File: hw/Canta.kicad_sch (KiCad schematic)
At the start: 50 parts, among them J1 USB_C_Receptacle_PowerOnly_6P, J101 Conn_01x01, J102 Conn_01x01, J103 Conn_01x01, J104 Conn_01x01, J105 Conn_01x01, J106 Conn_01x01, J107 Conn_01x01, J108 Conn_01x01, J109 Conn_01x01, J110 Conn_01x01, J111 Conn_01x01, J112 Conn_01x01, J2 Conn_01x04, U1 SPX3819M5-L-3-3, U2 PY32F003F18U6, U3 TM8211, U4 FM8002A, Y1 32MHz 12pF

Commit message: Fix thermal pad connection in PY32 symbol
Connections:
- net GND: now also U2.21 (PAD)
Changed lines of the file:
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@@
     (pin "8")
     (pin "9")
+    (pin "21")
     (instances
       (project "Canta"

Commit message: Layout, I think
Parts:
- removed J2: Conn_01x04, Canta_footprints:TestPoints_1x04_P2.0, symbol Connector_Generic:Conn_01x04
- added D1: Pink, LED_SMD:LED_0603_1608Metric, symbol Device:LED
- added J2: Conn_01x03, Canta_footprints:TestPoints_1x03_P2.0, symbol Connector_Generic:Conn_01x03
- added R3: 7.5k, Resistor_SMD:R_0402_1005Metric, symbol Device:R
- J101, J102, J103, J104, J105, J106, J107, J108, J109, J110: footprint TestPoint:TestPoint_Pad_4.0x4.0mm -> Canta_footprints:TouchPad_Keyboard
- J111, J112: footprint TestPoint:TestPoint_Pad_4.0x4.0mm -> Canta_footprints:TouchPad_Transpose
- JP1, JP2: footprint Jumper:SolderJumper-2_P1.3mm_Open_RoundedPad1.0x1.5mm -> Canta_footprints:SolderJumper-2_Open
- LS1: footprint Connector_PinHeader_2.00mm:PinHeader_1x02_P2.00mm_Vertical_SMD_Pin1Left -> Canta_footprints:Speaker_1x02_P2
- R6: renamed from R5; footprint Resistor_SMD:R_0402_1005Metric -> Potentiometer_SMD:Potentiometer_Bourns_TC33X_Vertical
- renumbered C5 to C4, C4 to C5, R3 to R4, R4 to R5
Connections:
- net +3.3V: now also D1.2 (A)
- net GND: now also J2.1 (Pin_1), R3.2
- net SWCLK: now also J2.2 (Pin_2)
- net SWDIO: now also J2.3 (Pin_3)
- new net: D1.1 (K), R3.1
- no-connect marks 3 -> 4

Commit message: Routing, I think
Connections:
- net BTN_01: now also U2.15 (PF2); no longer U2.16 (PA0)
- net BTN_02: now also U2.16 (PA0); no longer U2.18 (PA2)
- net BTN_03: now also U2.18 (PA2); no longer U2.19 (PA3)
- net BTN_04: now also U2.19 (PA3); no longer U2.20 (PA4)
- net BTN_05: now also U2.20 (PA4); no longer U2.1 (PA5)
- net BTN_06: now also U2.1 (PA5); no longer U2.2 (PA6)
- net BTN_07: now also U2.2 (PA6); no longer U2.3 (PA7)
- net BTN_08: now also U2.3 (PA7); no longer U2.5 (PA12)
- net BTN_09: now also U2.5 (PA12); no longer JP1.2 (B), U2.7 (PA13)
- net BTN_10: now also JP1.2 (B), U2.7 (PA13); no longer JP2.2 (B), U2.8 (PA14)
- net BTN_12: now also JP2.2 (B), U2.8 (PA14); no longer U2.15 (PF2)
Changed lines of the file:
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@@
     )
   )
-  (global_label "BTN_09" (shape bidirectional) (at 159.385 57.15 270) (fields_autoplaced)
+  (global_label "BTN_10" (shape bidirectional) (at 159.385 57.15 270) (fields_autoplaced)
     (effects (font (size 1.27 1.27)) (justify right))
     (property "Intersheetrefs" "${INTERSHEET_REFS}" (at 159.385 68.2012 90)
@@
     )
   )
-  (global_label "BTN_07" (shape bidirectional) (at 148.59 44.45 180) (fields_autoplaced)
+  (global_label "BTN_08" (shape bidirectional) (at 148.59 44.45 180) (fields_autoplaced)
     (effects (font (size 1.27 1.27)) (justify right))
     (property "Intersheetrefs" "${INTERSHEET_REFS}" (at 137.5388 44.45 0)
@@
     )
   )
-  (global_label "BTN_01" (shape bidirectional) (at 167.005 31.115 90) (fields_autoplaced)
+  (global_label "BTN_02" (shape bidirectional) (at 167.005 31.115 90) (fields_autoplaced)
     (effects (font (size 1.27 1.27)) (justify left))
     (property "Intersheetrefs" "${INTERSHEET_REFS}" (at 167.005 20.0638 90)
@@
     )
   )
-  (global_label "BTN_08" (shape bidirectional) (at 148.59 49.53 180) (fields_autoplaced)
+  (global_label "BTN_09" (shape bidirectional) (at 148.59 49.53 180) (fields_autoplaced)
     (effects (font (size 1.27 1.27)) (justify right))
     (property "Intersheetrefs" "${INTERSHEET_REFS}" (at 137.5388 49.53 0)
@@
     )
   )
-  (global_label "BTN_04" (shape bidirectional) (at 156.845 31.115 90) (fields_autoplaced)
+  (global_label "BTN_05" (shape bidirectional) (at 156.845 31.115 90) (fields_autoplaced)
     (effects (font (size 1.27 1.27)) (justify left))
     (property "Intersheetrefs" "${INTERSHEET_REFS}" (at 156.845 20.0638 90)
@@
     )
   )
-  (global_label "BTN_05" (shape bidirectional) (at 148.59 39.37 180) (fields_autoplaced)
+  (global_label "BTN_06" (shape bidirectional) (at 148.59 39.37 180) (fields_autoplaced)
     (effects (font (size 1.27 1.27)) (justify right))
     (property "Intersheetrefs" "${INTERSHEET_REFS}" (at 137.5388 39.37 0)
@@
     )
   )
-  (global_label "BTN_06" (shape bidirectional) (at 148.59 41.91 180) (fields_autoplaced)
+  (global_label "BTN_07" (shape bidirectional) (at 148.59 41.91 180) (fields_autoplaced)
     (effects (font (size 1.27 1.27)) (justify right))
     (property "Intersheetrefs" "${INTERSHEET_REFS}" (at 137.5388 41.91 0)
@@
     )
   )
-  (global_label "BTN_10" (shape bidirectional) (at 161.925 57.15 270) (fields_autoplaced)
+  (global_label "BTN_12" (shape bidirectional) (at 161.925 57.15 270) (fields_autoplaced)
     (effects (font (size 1.27 1.27)) (justify right))
     (property "Intersheetrefs" "${INTERSHEET_REFS}" (at 161.925 68.2012 90)
@@
     )
   )
-  (global_label "BTN_02" (shape bidirectional) (at 161.925 31.115 90) (fields_autoplaced)
+  (global_label "BTN_03" (shape bidirectional) (at 161.925 31.115 90) (fields_autoplaced)
     (effects (font (size 1.27 1.27)) (justify left))
     (property "Intersheetrefs" "${INTERSHEET_REFS}" (at 161.925 20.0638 90)
@@
     )
   )
-  (global_label "BTN_03" (shape bidirectional) (at 159.385 31.115 90) (fields_autoplaced)
+  (global_label "BTN_04" (shape bidirectional) (at 159.385 31.115 90) (fields_autoplaced)
     (effects (font (size 1.27 1.27)) (justify left))
     (property "Intersheetrefs" "${INTERSHEET_REFS}" (at 159.385 20.0638 90)
@@
     )
   )
-  (global_label "BTN_12" (shape bidirectional) (at 174.625 39.37 0) (fields_autoplaced)
+  (global_label "BTN_01" (shape bidirectional) (at 174.625 39.37 0) (fields_autoplaced)
     (effects (font (size 1.27 1.27)) (justify left))
     (property "Intersheetrefs" "${INTERSHEET_REFS}" (at 185.6762 39.37 0)

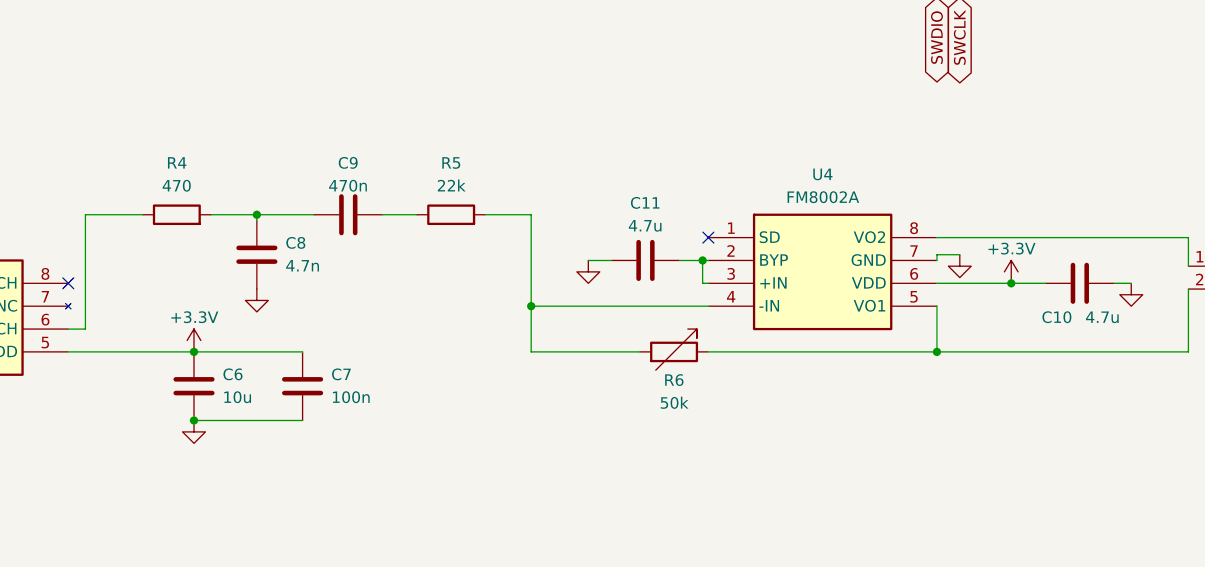
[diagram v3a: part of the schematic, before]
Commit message: Switch supplies of audio ICs to 5 V
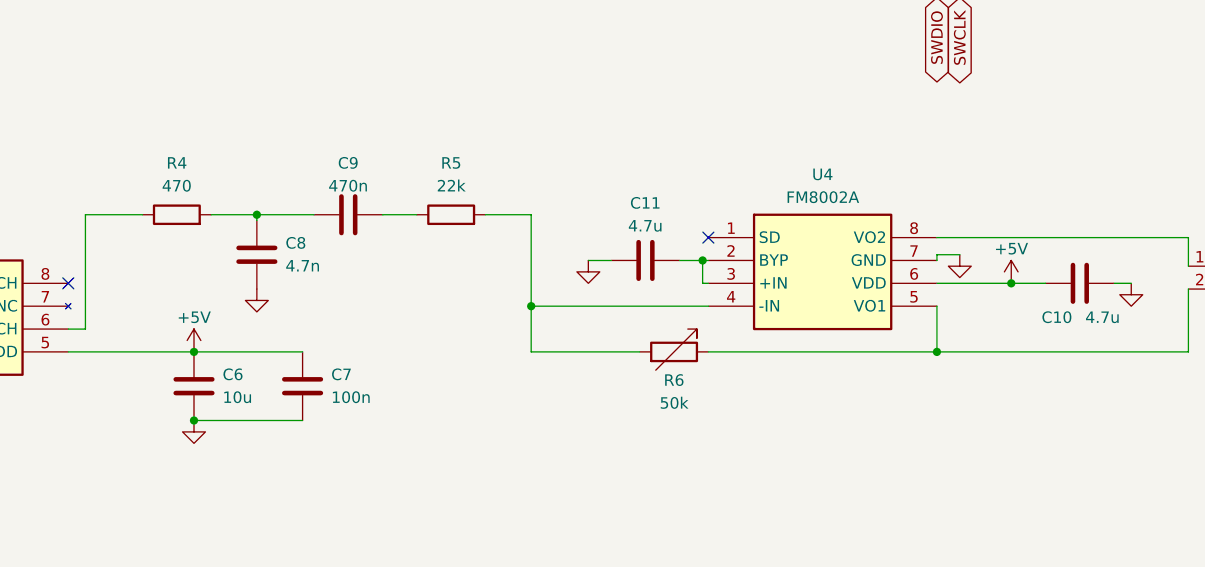
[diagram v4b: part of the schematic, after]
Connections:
- net +3.3V: no longer C10.1, C6.1, C7.1, U3.5 (VDD), U4.6 (VDD)
- net +5V: now also C10.1, C6.1, C7.1, U3.5 (VDD), U4.6 (VDD)

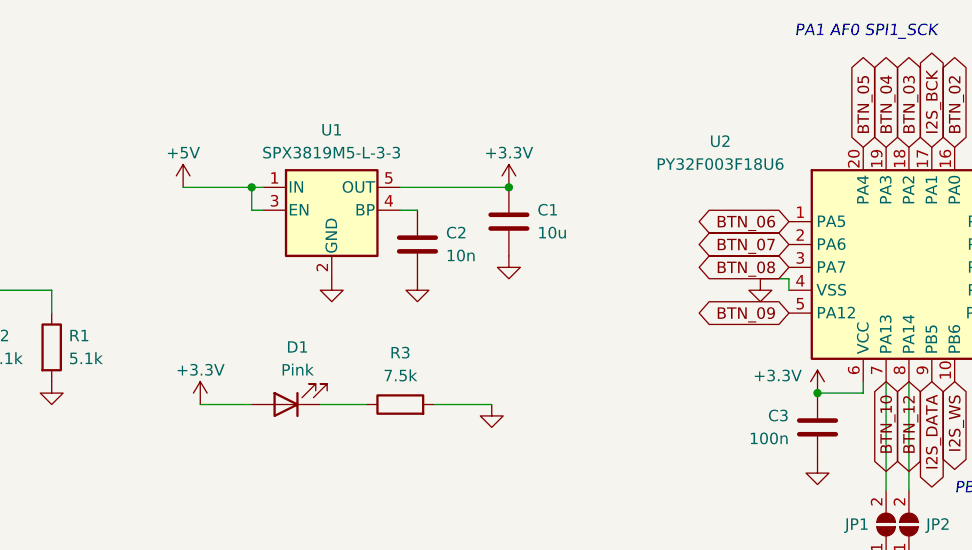
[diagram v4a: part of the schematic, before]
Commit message: Modify entire circuit to run on 5 V
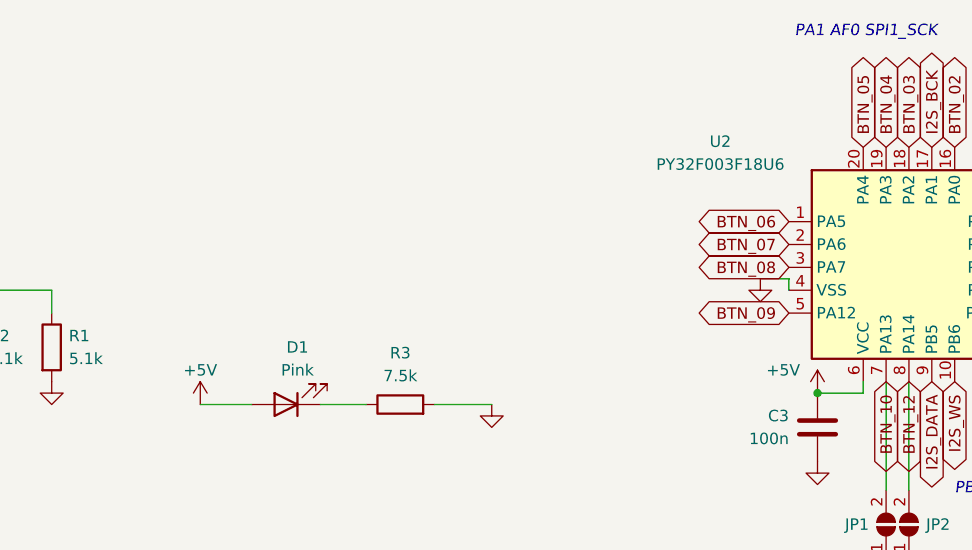
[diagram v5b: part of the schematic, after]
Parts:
- removed C1: 10u, Capacitor_SMD:C_0603_1608Metric, symbol Device:C
- removed C2: 10n, Capacitor_SMD:C_0402_1005Metric, symbol Device:C
- removed U1: SPX3819M5-L-3-3, Package_TO_SOT_SMD:SOT-23-5, symbol Regulator_Linear:SPX3819M5-L-3-3
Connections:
- net +3.3V: no longer C3.1, D1.2 (A), U2.6 (VCC)
- net +5V: now also C3.1, D1.2 (A), U2.6 (VCC)

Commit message: Update silkscreen
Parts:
- R3: value 7.5k -> 10k
- renumbered C3 to C1, C4 to C2, C5 to C3, C6 to C4, C7 to C5, C8 to C6, C9 to C7, C10 to C8, C11 to C9, U2 to U1, U3 to U2, U4 to U3
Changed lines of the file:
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@@
       (effects (font (size 1.27 1.27)))
     )
-    (property "Value" "7.5k" (at 105.41 56.515 90)
+    (property "Value" "10k" (at 105.41 56.515 90)
       (effects (font (size 1.27 1.27)))
     )
@@
   (symbol (lib_id "Device:C") (at 88.9 120.015 0) (unit 1)
     (in_bom yes) (on_board yes) (dnp no)
-    (property "Reference" "C7" (at 92.075 118.745 0)
+    (property "Reference" "C5" (at 92.075 118.745 0)
       (effects (font (size 1.27 1.27)) (justify left))
     )
@@
       (project "Canta"
         (path "/0da9ae68-938f-47fa-aa31-df1300665123"
-          (reference "C7") (unit 1)
+          (reference "C5") (unit 1)
         )
       )
@@
   (symbol (lib_id "Device:C") (at 76.835 120.015 0) (unit 1)
     (in_bom yes) (on_board yes) (dnp no)
-    (property "Reference" "C6" (at 80.01 118.745 0)
+    (property "Reference" "C4" (at 80.01 118.745 0)
       (effects (font (size 1.27 1.27)) (justify left))
     )
@@
       (project "Canta"
         (path "/0da9ae68-938f-47fa-aa31-df1300665123"
-          (reference "C6") (unit 1)
+          (reference "C4") (unit 1)
         )
       )
@@
   (symbol (lib_id "Device:C") (at 175.26 108.585 90) (unit 1)
     (in_bom yes) (on_board yes) (dnp no)
-    (property "Reference" "C10" (at 172.72 112.395 90)
+    (property "Reference" "C8" (at 172.72 112.395 90)
       (effects (font (size 1.27 1.27)))
     )
@@
       (project "Canta"
         (path "/0da9ae68-938f-47fa-aa31-df1300665123"
-          (reference "C10") (unit 1)
+          (reference "C8") (unit 1)
         )
       )
@@
   (symbol (lib_id "Canta_symbols:PY32F003F18U6TR") (at 161.925 44.45 0) (unit 1)
     (in_bom yes) (on_board yes) (dnp no)
-    (property "Reference" "U2" (at 140.97 30.48 0)
+    (property "Reference" "U1" (at 140.97 30.48 0)
       (effects (font (size 1.27 1.27)))
     )
@@
       (project "Canta"
         (path "/0da9ae68-938f-47fa-aa31-df1300665123"
-          (reference "U2") (unit 1)
+          (reference "U1") (unit 1)
         )
       )
@@
   (symbol (lib_id "Device:C") (at 151.765 62.23 0) (mirror y) (unit 1)
     (in_bom yes) (on_board yes) (dnp no)
-    (property "Reference" "C3" (at 148.59 60.96 0)
+    (property "Reference" "C1" (at 148.59 60.96 0)
       (effects (font (size 1.27 1.27)) (justify left))
     )
@@
       (project "Canta"
         (path "/0da9ae68-938f-47fa-aa31-df1300665123"
-          (reference "C3") (unit 1)
+          (reference "C1") (unit 1)
         )
       )
@@
   (symbol (lib_id "Device:C") (at 127 106.045 90) (unit 1)
     (in_bom yes) (on_board yes) (dnp no)
-    (property "Reference" "C11" (at 127 99.695 90)
+    (property "Reference" "C9" (at 127 99.695 90)
       (effects (font (size 1.27 1.27)))
     )
@@
       (project "Canta"
         (path "/0da9ae68-938f-47fa-aa31-df1300665123"
-          (reference "C11") (unit 1)
+          (reference "C9") (unit 1)
         )
       )
@@
   (symbol (lib_id "Device:C") (at 83.82 105.41 0) (unit 1)
     (in_bom yes) (on_board yes) (dnp no)
-    (property "Reference" "C8" (at 86.995 104.14 0)
+    (property "Reference" "C6" (at 86.995 104.14 0)
       (effects (font (size 1.27 1.27)) (justify left))
     )
@@
       (project "Canta"
         (path "/0da9ae68-938f-47fa-aa31-df1300665123"
-          (reference "C8") (unit 1)
+          (reference "C6") (unit 1)
         )
       )
@@
   (symbol (lib_id "Device:C") (at 212.725 46.99 90) (mirror x) (unit 1)
     (in_bom yes) (on_board yes) (dnp no)
-    (property "Reference" "C4" (at 210.185 50.8 90)
+    (property "Reference" "C2" (at 210.185 50.8 90)
       (effects (font (size 1.27 1.27)))
     )
@@
       (project "Canta"
         (path "/0da9ae68-938f-47fa-aa31-df1300665123"
-          (reference "C4") (unit 1)
+          (reference "C2") (unit 1)
         )
       )
@@
   (symbol (lib_id "Device:C") (at 212.725 38.1 90) (unit 1)
     (in_bom yes) (on_board yes) (dnp no)
-    (property "Reference" "C5" (at 210.185 34.29 90)
+    (property "Reference" "C3" (at 210.185 34.29 90)
       (effects (font (size 1.27 1.27)))
     )
@@
       (project "Canta"
         (path "/0da9ae68-938f-47fa-aa31-df1300665123"
-          (reference "C5") (unit 1)
+          (reference "C3") (unit 1)
         )
       )
@@
   )
   (symbol (lib_id "TM8211:TM8211") (at 37.465 108.585 0) (unit 1)
-    (in_bom yes) (on_board yes) (dnp no) (fields_autoplaced)
-    (property "Reference" "U3" (at 50.165 100.965 0)
+    (in_bom yes) (on_board yes) (dnp no)
+    (property "Reference" "U2" (at 50.165 100.965 0)
       (effects (font (size 1.27 1.27)))
     )
@@
       (project "Canta"
         (path "/0da9ae68-938f-47fa-aa31-df1300665123"
-          (reference "U3") (unit 1)
+          (reference "U2") (unit 1)
         )
       )
@@
   (symbol (lib_id "Device:C") (at 93.98 100.965 90) (unit 1)
     (in_bom yes) (on_board yes) (dnp no)
-    (property "Reference" "C9" (at 93.98 95.25 90)
+    (property "Reference" "C7" (at 93.98 95.25 90)
       (effects (font (size 1.27 1.27)))
     )
@@
       (project "Canta"
         (path "/0da9ae68-938f-47fa-aa31-df1300665123"
-          (reference "C9") (unit 1)
+          (reference "C7") (unit 1)
         )
       )
@@
   (symbol (lib_id "MD8002A:FM8002A") (at 133.985 103.505 0) (unit 1)
     (in_bom yes) (on_board yes) (dnp no) (fields_autoplaced)
-    (property "Reference" "U4" (at 146.685 96.52 0)
+    (property "Reference" "U3" (at 146.685 96.52 0)
       (effects (font (size 1.27 1.27)))
     )
@@
       (project "Canta"
         (path "/0da9ae68-938f-47fa-aa31-df1300665123"
-          (reference "U4") (unit 1)
-        )
-      )
+          (reference "U3") (unit 1)
+        )
+      )
